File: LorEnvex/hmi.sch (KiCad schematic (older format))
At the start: 30 parts

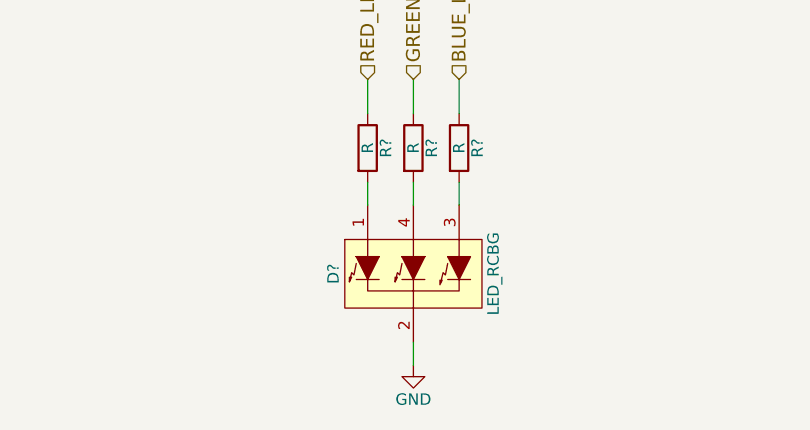
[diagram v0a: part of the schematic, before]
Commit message: added touchscreen controller to bom.txt.
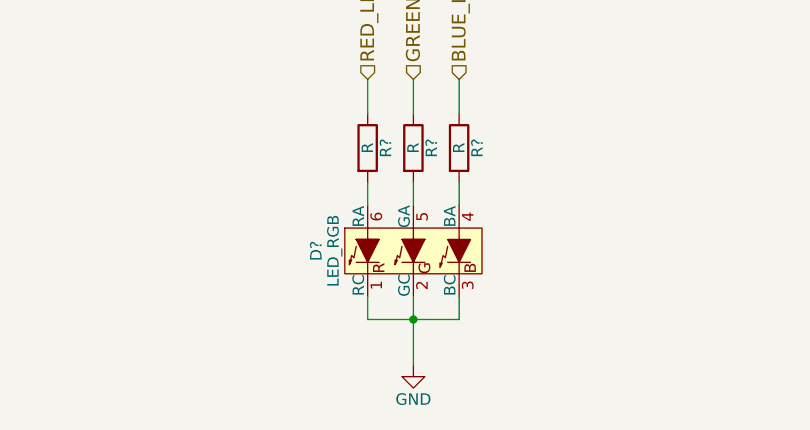
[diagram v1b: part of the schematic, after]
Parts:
- removed D?: LED_RCBG, symbol LED_RCBG
- removed SW?: TSWB-3N-CB222, symbol TSWB-3N-CB222
- added D?: LED_RGB, symbol LED_RGB
- added SW?: TSWB-3N-CB222, symbol TSWB-3N-CB222
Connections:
- net GND: now also D?.1 (RC), D?.2 (GC), D?.3 (BC), SW?.~ (S5)
- net at R?.2: now also D?.6 (RA)
- net at R?.2: now also D?.4 (BA)
- net at R?.2: now also D?.5 (GA)
- net at C?.1, R?.1, R?.2: now also SW?.~ (S5) (x7)
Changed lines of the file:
@@
 EESchema Schematic File Version 2
+LIBS:LorEnvex-rescue
 LIBS:power
 LIBS:device
@@
 LIBS:ac-dc
 LIBS:actel
+LIBS:Altera
 LIBS:analog_devices
 LIBS:brooktre
 LIBS:cmos_ieee
 LIBS:dc-dc
+LIBS:diode
 LIBS:elec-unifil
+LIBS:ESD_Protection
 LIBS:ftdi
 LIBS:gennum
@@
 LIBS:hc11
 LIBS:ir
+LIBS:Lattice
 LIBS:logo
+LIBS:maxim
 LIBS:microchip_dspic33dsc
 LIBS:microchip_pic10mcu
@@
 LIBS:nxp_armmcu
 LIBS:onsemi
+LIBS:Oscillators
 LIBS:powerint
+LIBS:Power_Management
 LIBS:pspice
 LIBS:references
@@
 LIBS:ttl_ieee
 LIBS:video
+LIBS:Xicor
+LIBS:Zilog
 LIBS:Symbols_DCDC-ACDC-Converter_RevC_20Jul2012
 LIBS:Symbols_EN60617_13Mar2013
@@
 $EndComp
 $Comp
-L LED_RCBG D?
-U 1 1 571D3F98
-P 3150 4250
-F 0 "D?" H 3150 4600 50  0000 C CNN
-F 1 "LED_RCBG" H 3150 3900 50  0000 C CNN
-F 2 "" H 3150 4200 50  0000 C CNN
-F 3 "" H 3150 4200 50  0000 C CNN
-	1    3150 4250
-	0    -1   1    0
-$EndComp
-$Comp
-L TSWB-3N-CB222 SW?
-U 1 1 571D43E9
-P 6200 1700
-F 0 "SW?" H 6200 1050 60  0000 C CNN
-F 1 "TSWB-3N-CB222" H 6200 1200 60  0000 C CNN
-F 2 "" H 6450 1750 60  0000 C CNN
-F 3 "" H 6450 1750 60  0000 C CNN
-	1    6200 1700
-	1    0    0    -1
-$EndComp
-$Comp
 L R R?
 U 1 1 571D45DC
@@
 	3350 3850 3350 3950
 Wire Wire Line
-	3150 4550 3150 4650
+	3150 4350 3150 4650
 Wire Wire Line
 	2950 3400 2950 3550
@@
 Wire Wire Line
 	8700 2000 9050 2000
+$Comp
+L LED_RGB D?
+U 1 1 571F8E93
+P 3150 4150
+F 0 "D?" H 3150 4575 50  0000 C CNN
+F 1 "LED_RGB" H 3150 4500 50  0000 C CNN
+F 2 "" H 3150 4100 50  0000 C CNN
+F 3 "" H 3150 4100 50  0000 C CNN
+	1    3150 4150
+	0    -1   -1   0
+$EndComp
+Wire Wire Line
+	2950 4350 2950 4450
+Wire Wire Line
+	2950 4450 3350 4450
+Wire Wire Line
+	3350 4450 3350 4350
+Connection ~ 3150 4450
+$Comp
+L TSWB-3N-CB222 SW?
+U 1 1 571FB9E4
+P 6200 1700
+F 0 "SW?" H 6200 1050 60  0000 C CNN
+F 1 "TSWB-3N-CB222" H 6200 1200 60  0000 C CNN
+F 2 "" H 6450 1750 60  0000 C CNN
+F 3 "" H 6450 1750 60  0000 C CNN
+	1    6200 1700
+	1    0    0    -1
+$EndComp
 $EndSCHEMATC

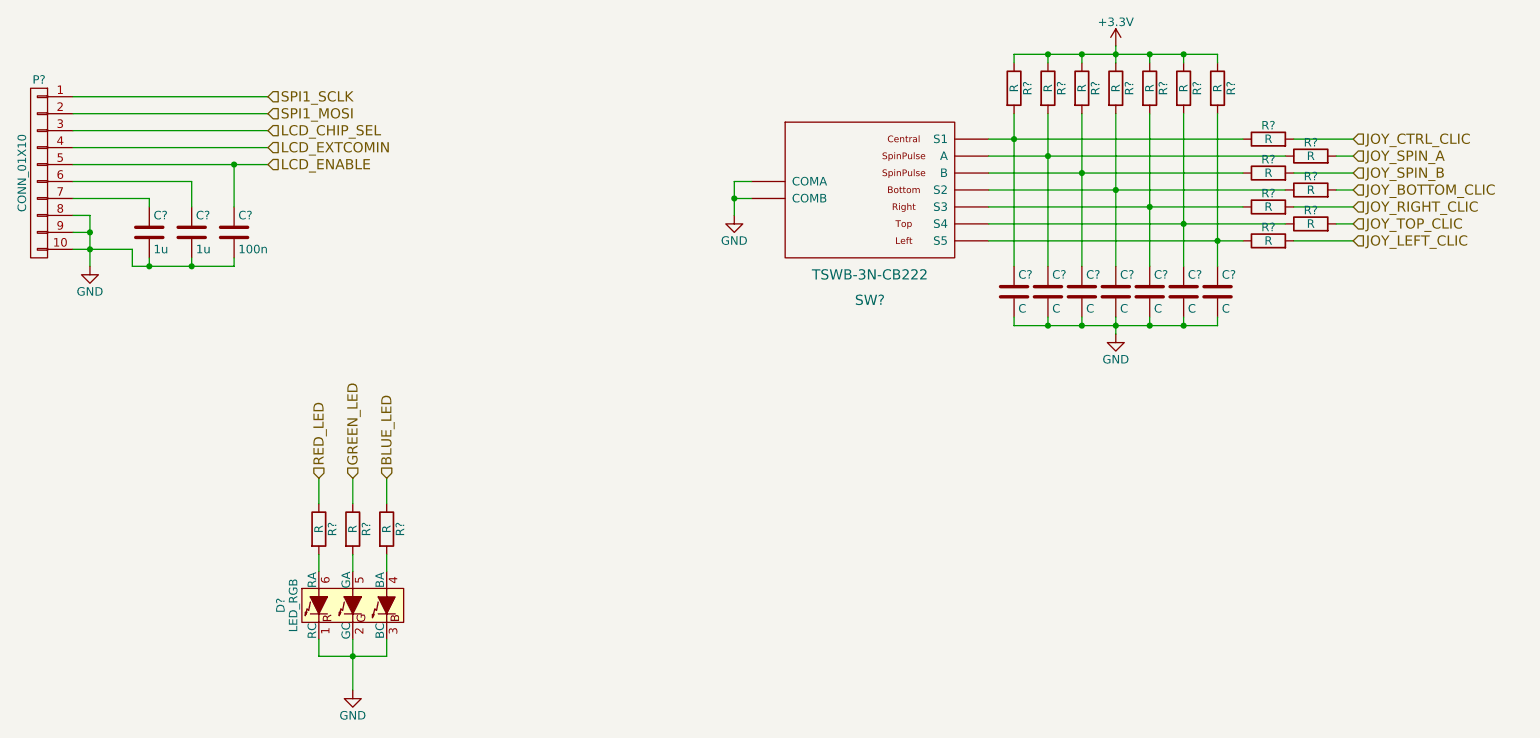
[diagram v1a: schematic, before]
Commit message: created new component for the touchscreen controller
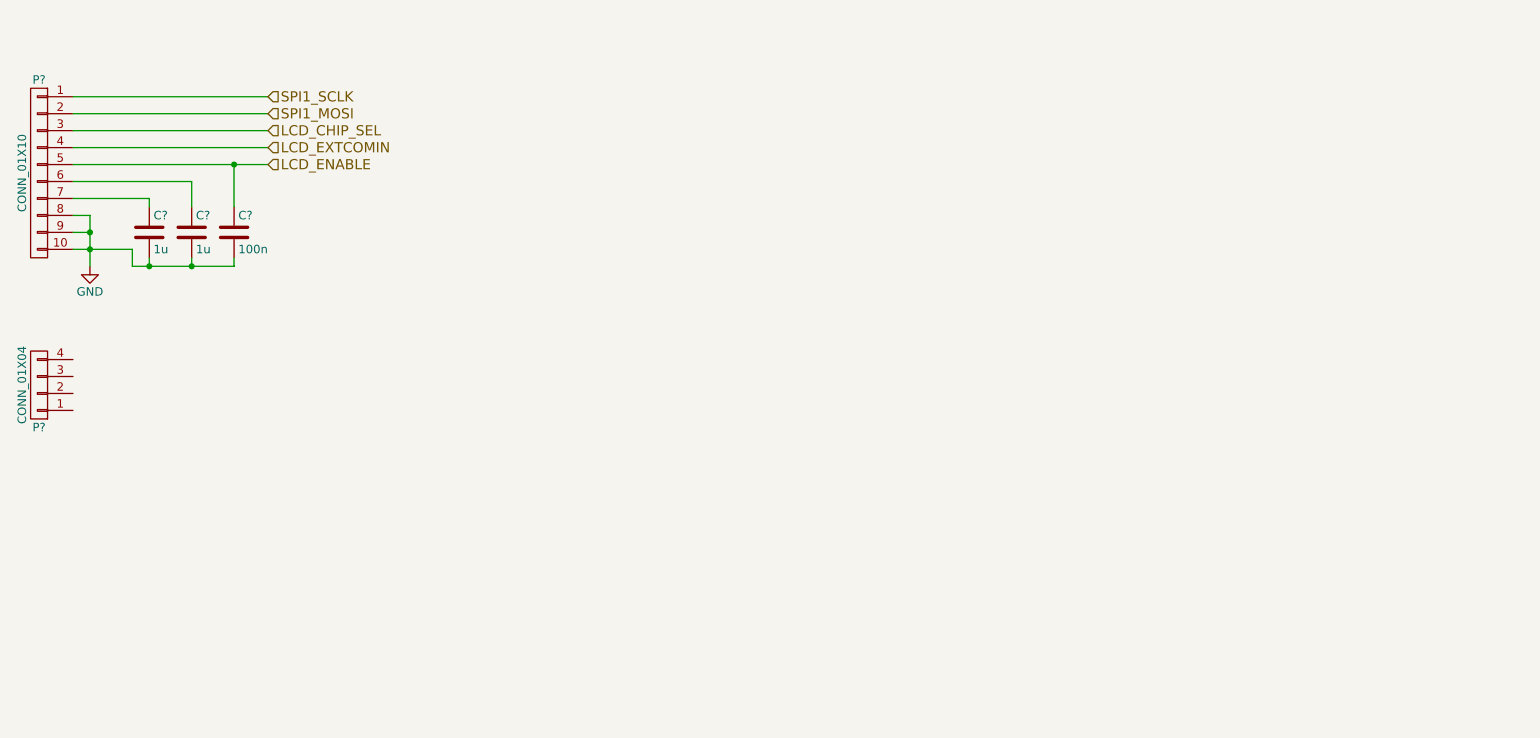
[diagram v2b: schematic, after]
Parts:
- removed C? (x7): C, symbol C
- removed D?: LED_RGB, symbol LED_RGB
- removed R? (x17): R, symbol R
- removed SW?: TSWB-3N-CB222, symbol TSWB-3N-CB222
- added P?: CONN_01X04, symbol CONN_01X04
